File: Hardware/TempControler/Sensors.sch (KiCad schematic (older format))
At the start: 0 parts

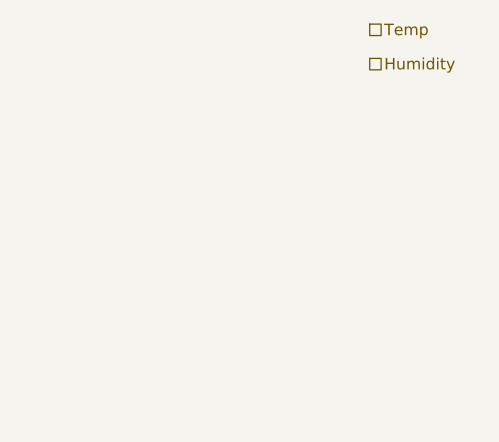
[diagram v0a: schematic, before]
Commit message: Schematic Complete
DRC - Done
Schematic - Done
Values - Done
Part Selection - In Progress
Footprint assignment- In Progress
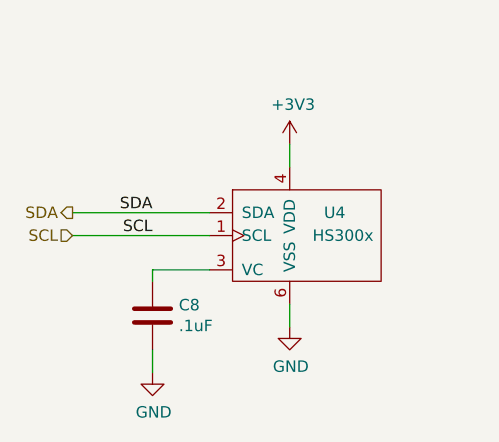
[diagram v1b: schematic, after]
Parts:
- added C8: .1uF, Capacitor_SMD:C_0805_2012Metric, symbol Device:C
- added U4: HS300x, symbol Misc:HS300x
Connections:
- new net: C8.1, U4.3 (VC)
- new net +3V3: U4.4 (VDD)
- new net GND: C8.2, U4.6 (VSS)
- new net SCL: U4.1 (SCL)
- new net SDA: U4.2 (SDA)
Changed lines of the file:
@@
 $Descr USLetter 11000 8500
 encoding utf-8
-Sheet 5 7
+Sheet 5 8
 Title ""
 Date ""
@@
 Comment4 ""
 $EndDescr
-Text HLabel 4400 3800 2    50   UnSpc ~ 0
-Temp
-Text HLabel 4400 3950 2    50   UnSpc ~ 0
-Humidity
+Text HLabel 3100 4600 0    50   Output ~ 0
+SDA
+Text HLabel 3100 4700 0    50   Input ~ 0
+SCL
+$Comp
+L Misc:HS300x U4
+U 1 1 6308BB19
+P 4250 4650
+F 0 "U4" H 4200 4700 50  0000 L CNN
+F 1 "HS300x" H 4150 4600 50  0000 L CNN
+F 2 "" H 4250 4650 50  0001 C CNN
+F 3 "https://www.mouser.com/datasheet/2/698/REN_HS300x_Datasheet_DST_20210809-1997723.pdf" H 4250 4650 50  0001 C CNN
+F 4 "972-HS3004" H 4594 4509 50  0001 L CNN "Mouser"
+	1    4250 4650
+	1    0    0    -1
+$EndComp
+$Comp
+L Device:C C8
+U 1 1 6308CC8C
+P 3450 5050
+F 0 "C8" H 3565 5096 50  0000 L CNN
+F 1 ".1uF" H 3565 5005 50  0000 L CNN
+F 2 "Capacitor_SMD:C_0805_2012Metric" H 3488 4900 50  0001 C CNN
+F 3 "~" H 3450 5050 50  0001 C CNN
+	1    3450 5050
+	1    0    0    -1
+$EndComp
+$Comp
+L power:+3V3 #PWR0120
+U 1 1 6308E5F1
+P 4050 4300
+F 0 "#PWR0120" H 4050 4150 50  0001 C CNN
+F 1 "+3V3" H 4065 4473 50  0000 C CNN
+F 2 "" H 4050 4300 50  0001 C CNN
+F 3 "" H 4050 4300 50  0001 C CNN
+	1    4050 4300
+	1    0    0    -1
+$EndComp
+$Comp
+L power:GND #PWR0121
+U 1 1 6308EE2D
+P 4050 5100
+F 0 "#PWR0121" H 4050 4850 50  0001 C CNN
+F 1 "GND" H 4055 4927 50  0000 C CNN
+F 2 "" H 4050 5100 50  0001 C CNN
+F 3 "" H 4050 5100 50  0001 C CNN
+	1    4050 5100
+	1    0    0    -1
+$EndComp
+$Comp
+L power:GND #PWR0122
+U 1 1 6308F83B
+P 3450 5300
+F 0 "#PWR0122" H 3450 5050 50  0001 C CNN
+F 1 "GND" H 3455 5127 50  0000 C CNN
+F 2 "" H 3450 5300 50  0001 C CNN
+F 3 "" H 3450 5300 50  0001 C CNN
+	1    3450 5300
+	1    0    0    -1
+$EndComp
+Text Label 3450 4600 2    50   ~ 0
+SDA
+Text Label 3450 4700 2    50   ~ 0
+SCL
+Wire Wire Line
+	3700 4600 3100 4600
+Wire Wire Line
+	3700 4700 3100 4700
+Wire Wire Line
+	3700 4850 3450 4850
+Wire Wire Line
+	3450 4850 3450 4900
+Wire Wire Line
+	3450 5200 3450 5300
+Wire Wire Line
+	4050 5000 4050 5100
+Wire Wire Line
+	4050 4400 4050 4300
 $EndSCHEMATC

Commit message: All Part Numbers Selected
Next step select all footprints
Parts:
- C8: Mouser (none) -> 80-C0805C104K5R
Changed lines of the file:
@@
 F 1 ".1uF" H 3565 5005 50  0000 L CNN
 F 2 "Capacitor_SMD:C_0805_2012Metric" H 3488 4900 50  0001 C CNN
-F 3 "~" H 3450 5050 50  0001 C CNN
+F 3 "https://www.mouser.com/datasheet/2/212/KEM_C1002_X7R_SMD-1102033.pdf" H 3450 5050 50  0001 C CNN
+F 4 "80-C0805C104K5R" H 3450 5050 50  0001 C CNN "Mouser"
 	1    3450 5050
 	1    0    0    -1

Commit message: Footprints selected
On to board design
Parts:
- U4: footprint (none) -> xPackage_LGA:LGA-6_2.4x3mm_P1mm; symbol Misc:HS300x -> Sensors:HS300x
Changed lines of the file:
@@
 SCL
 $Comp
-L Misc:HS300x U4
+L Sensors:HS300x U4
 U 1 1 6308BB19
 P 4250 4650
 F 0 "U4" H 4200 4700 50  0000 L CNN
 F 1 "HS300x" H 4150 4600 50  0000 L CNN
-F 2 "" H 4250 4650 50  0001 C CNN
+F 2 "xPackage_LGA:LGA-6_2.4x3mm_P1mm" H 4250 4650 50  0001 C CNN
 F 3 "https://www.mouser.com/datasheet/2/698/REN_HS300x_Datasheet_DST_20210809-1997723.pdf" H 4250 4650 50  0001 C CNN
 F 4 "972-HS3004" H 4594 4509 50  0001 L CNN "Mouser"
